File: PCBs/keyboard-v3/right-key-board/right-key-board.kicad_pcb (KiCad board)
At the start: 2 copper layers, 115 x 86 mm, 71 parts, among them J301 F31Z1A7H111008, Q201 DMN21D2UFB-7B, SW201 SW_DIP_x01, SW202 SW_DIP_x01, SW203 SW_DIP_x01, SW204 SW_DIP_x01, SW205 SW_DIP_x01, SW206 SW_DIP_x01, SW207 SW_DIP_x01, SW208 SW_DIP_x01, SW209 SW_DIP_x01, SW210 SW_DIP_x01, SW211 SW_DIP_x01, SW212 SW_DIP_x01, SW213 SW_DIP_x01, SW214 SW_DIP_x01, SW215 SW_DIP_x01, SW216 SW_DIP_x01, SW217 SW_DIP_x01, SW218 SW_DIP_x01, SW219 SW_DIP_x01, SW220 SW_DIP_x01, SW221 SW_DIP_x01, SW222 SW_DIP_x01, SW223 SW_DIP_x01, SW224 SW_DIP_x01, U301 STM32U031C6Ux

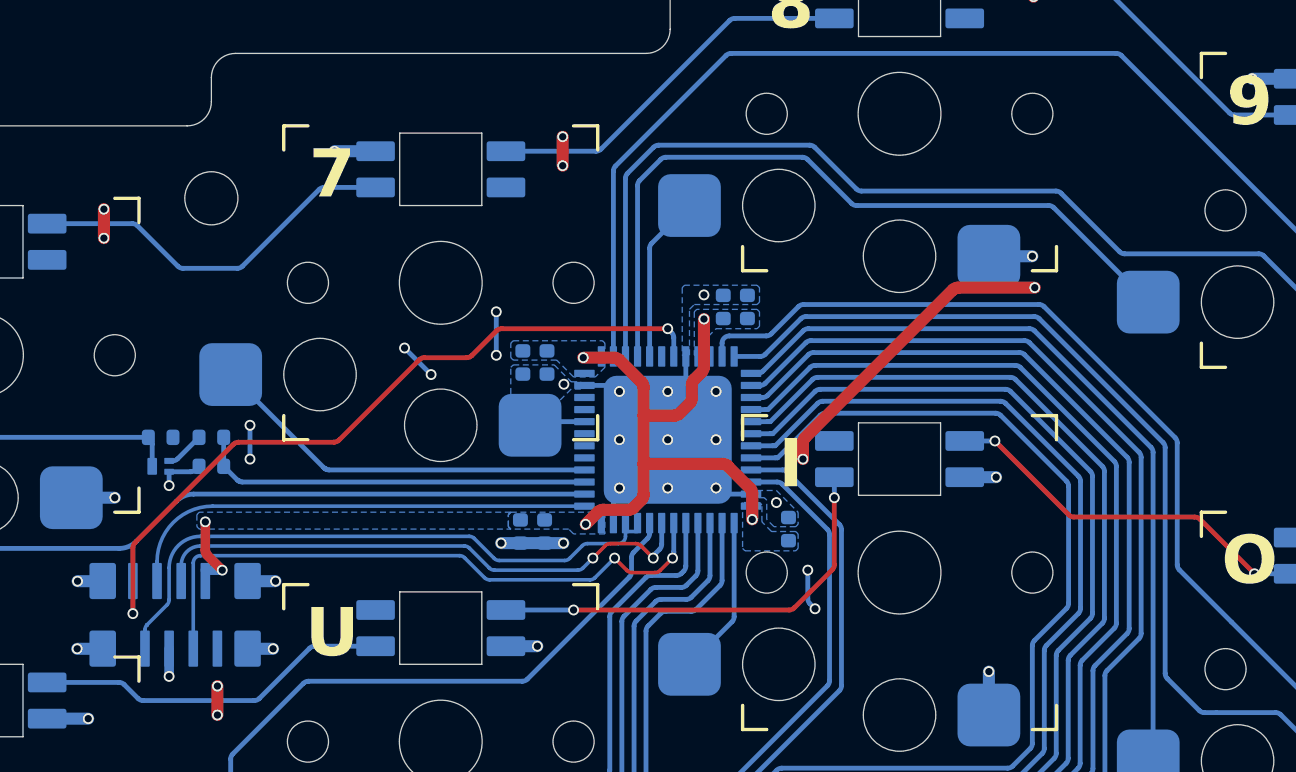
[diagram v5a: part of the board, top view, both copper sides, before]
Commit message: Finished debug breakout board and added 5V voltage sensing to key board
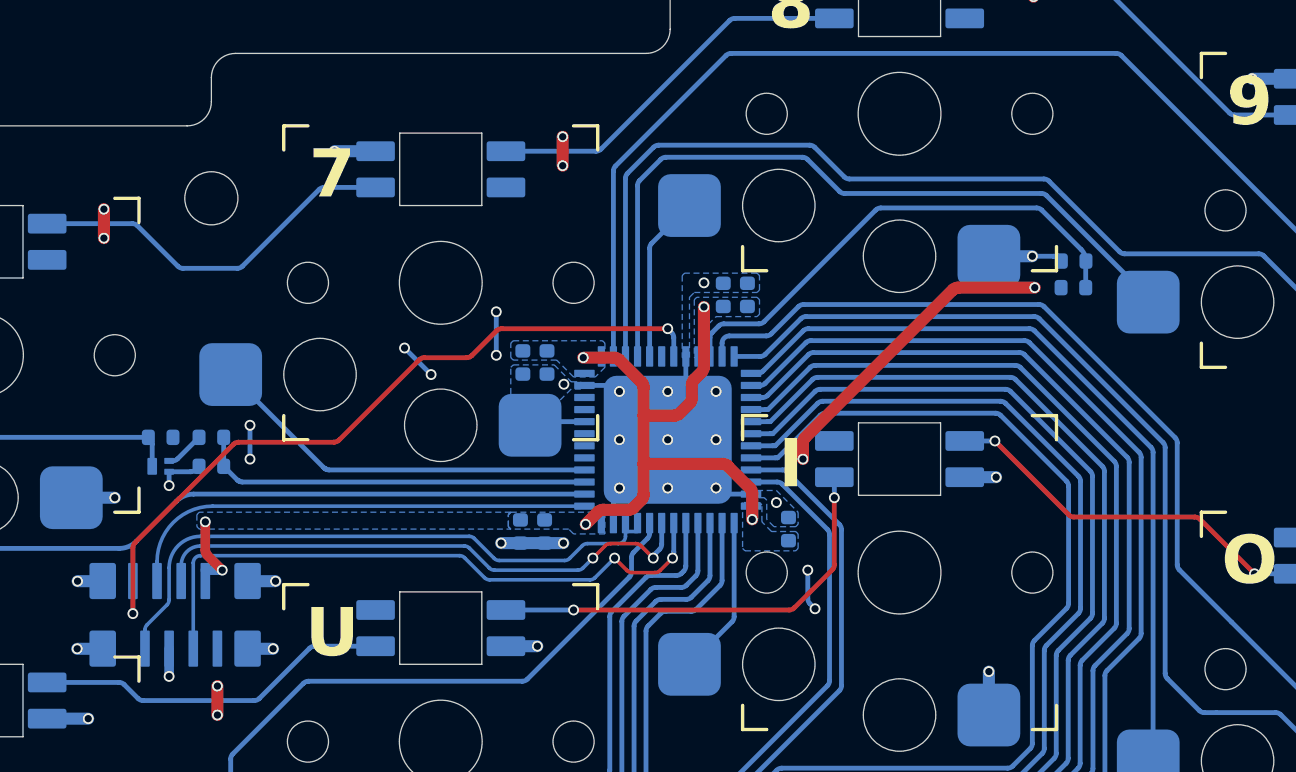
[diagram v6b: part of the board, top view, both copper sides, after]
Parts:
- added R6: 10k, project_footprints:R_0402, B.Cu at (149.7, 66.7)
- added R7: 2k2, project_footprints:R_0402, B.Cu at (149.7, 65.6)
- moved C301 0.50 mm to (135.2, 67.0)
- moved C302 0.50 mm to (136.2, 67.0)
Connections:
- U301 pad 10: unconnected-(U301-PA0-Pad10) -> /MCU/5V_SENSE
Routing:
- net /MCU/5V_SENSE: track 0.00 -> 20.7 mm
- net GND: track 139.3 -> 140.6 mm

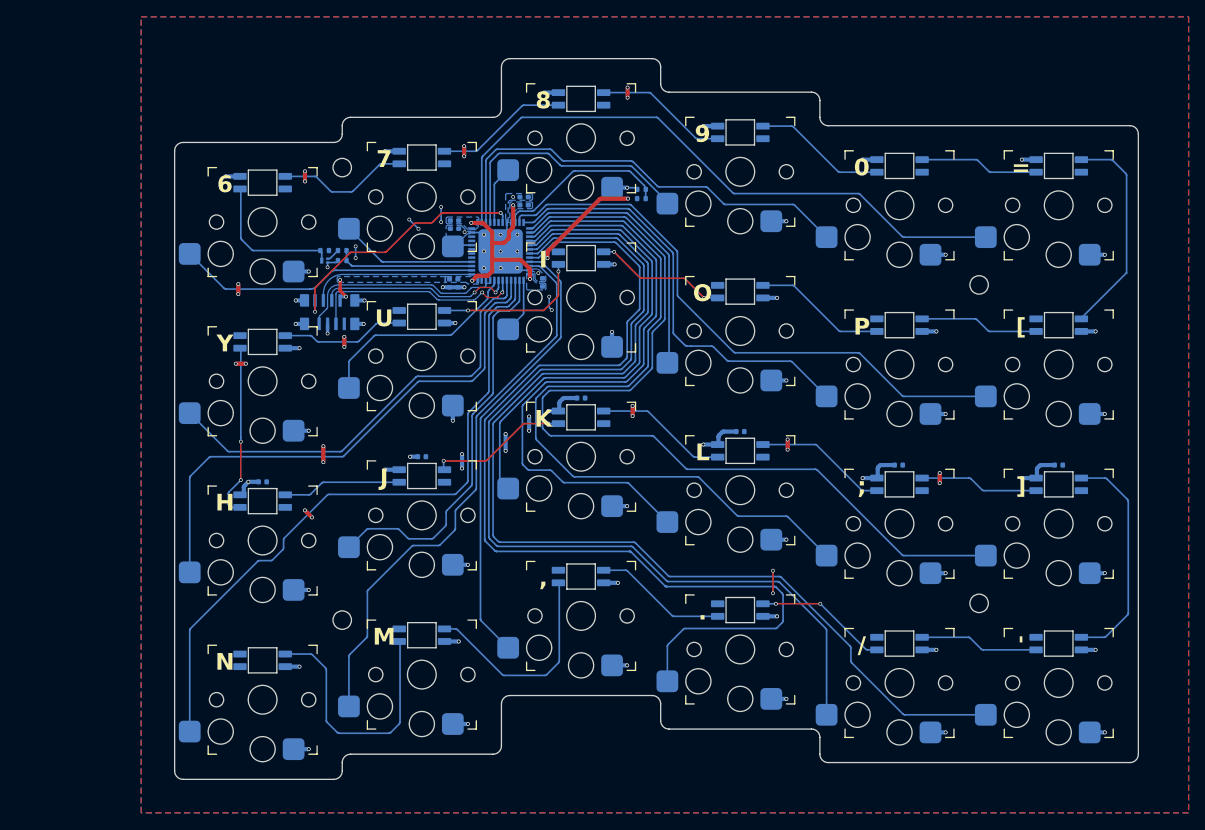
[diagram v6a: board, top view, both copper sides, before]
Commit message: Left key board done
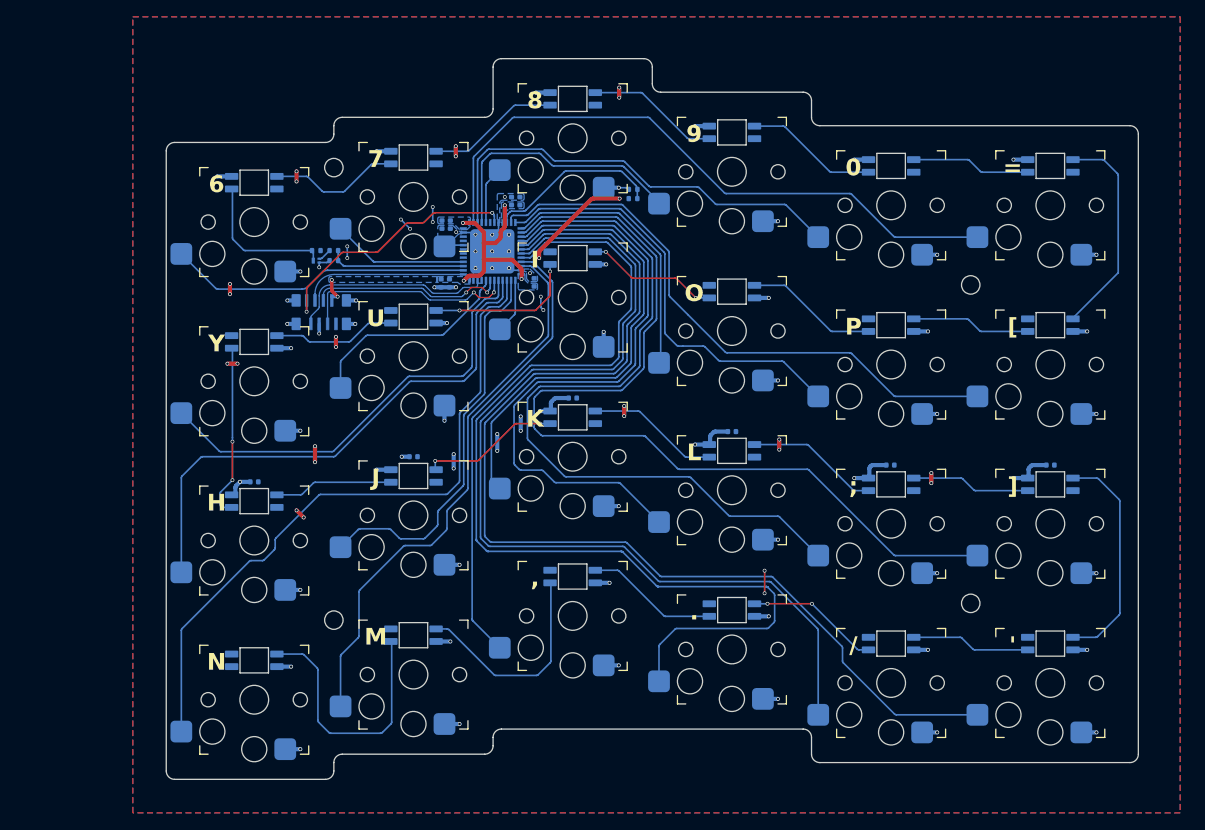
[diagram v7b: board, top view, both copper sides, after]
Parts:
- H101, H102, H103, H104: moved to B.Cu
- moved C201 1.00 mm to (103.5, 100.5)
- moved C202 1.00 mm to (198.5, 98.5)
- moved C203 1.00 mm to (179.4, 98.5)
- moved C204 1.00 mm to (160.5, 94.5)
- moved C205 1.00 mm to (141.5, 90.5)
- moved C206 1.00 mm to (122.5, 97.5)
- moved C301 1.00 mm to (134.2, 67.0)
- moved C302 1.00 mm to (135.2, 67.0)
- moved C303 1.00 mm to (126.8, 76.8)
- moved C304 1.00 mm to (136.9, 76.7)
- moved C305 1.00 mm to (125.9, 69.8)
- moved C306 1.00 mm to (125.8, 76.8)
- moved C307 1.00 mm to (126.9, 69.8)
- moved D201 1.00 mm to (103.5, 64.8)
- moved D202 1.00 mm to (122.5, 61.8)
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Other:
- board size 115 x 86 mm -> 116 x 86 mm

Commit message: Keyboard v3 hardware done
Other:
- board text added: "Keyboard v3 Right Key Board Ben Smith 2026"
